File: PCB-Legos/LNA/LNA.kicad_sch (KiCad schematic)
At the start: 42 parts, among them J1 Conn_Coaxial, J2 Conn_Coaxial, J3 Conn_Coaxial, J4 474-PRT-00587, U1 LP2985XX-N, U2 LNA-TP3M9037, U3 QPQ1907, U4 LP2985XX-N, U5 LNA-TP3M9037, U6 QPQ1907

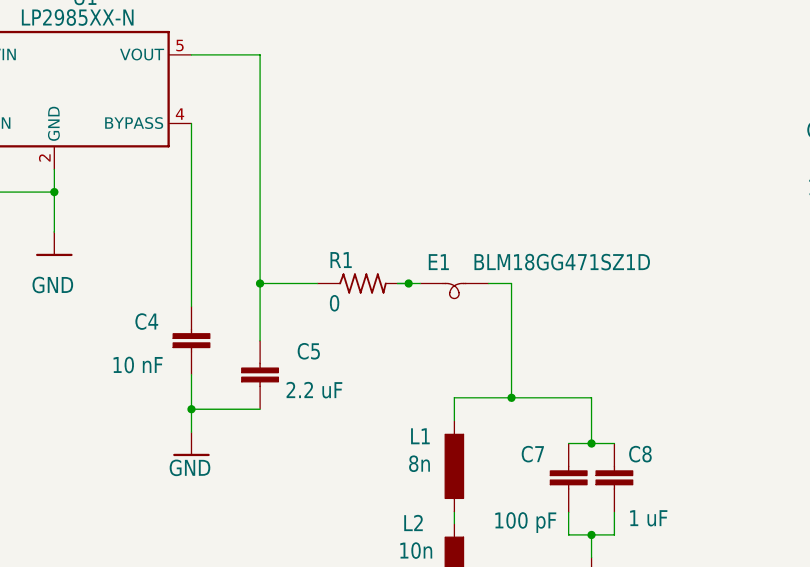
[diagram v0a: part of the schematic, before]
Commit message: 50 Ohm microstrip
Test boards with a through, impedance matching network and 50ohm load test
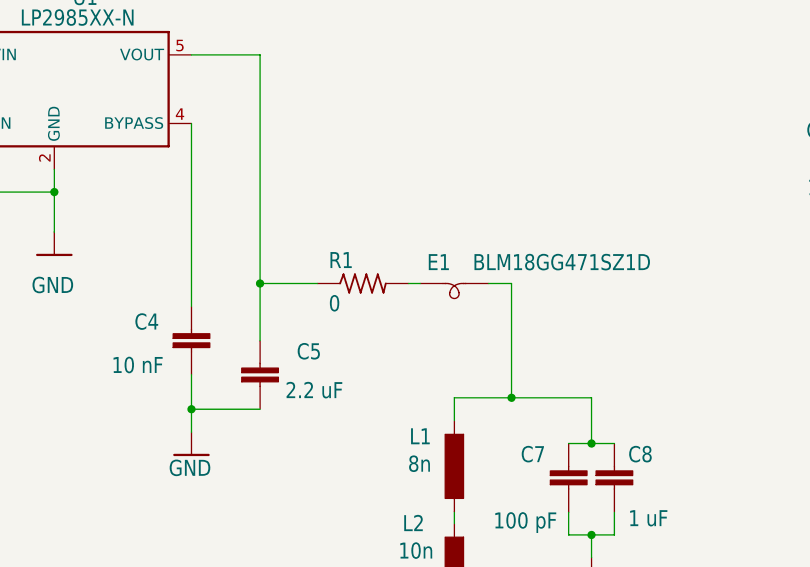
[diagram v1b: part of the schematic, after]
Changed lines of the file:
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@@
   (junction (at 95.25 86.36) (diameter 0) (color 0 0 0 0)
-  )
-  (junction (at 83.82 73.66) (diameter 0) (color 0 0 0 0)
   )
   (junction (at 29.21 55.88) (diameter 0) (color 0 0 0 0)
@@
     (stroke (width 0) (type default) (color 0 0 0 0))
   )
-  (wire (pts (xy 82.55 73.66) (xy 83.82 73.66))
-    (stroke (width 0) (type default) (color 0 0 0 0))
-  )
